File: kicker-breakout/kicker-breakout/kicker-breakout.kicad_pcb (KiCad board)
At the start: 2 copper layers, 43 x 37.8 mm, 16 parts, among them J1 POWER, J2 DEV_BOARD, J3 KICKER_CONNECTION, Q1 BSS84

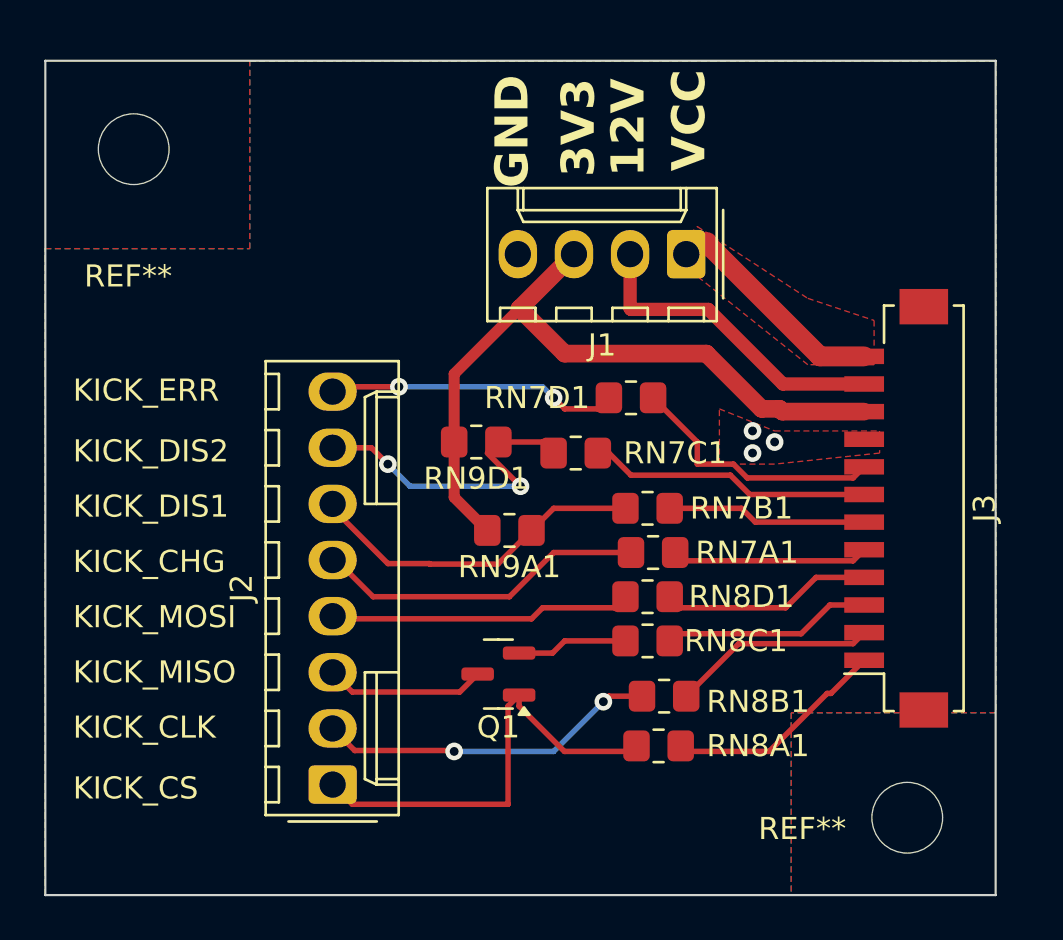
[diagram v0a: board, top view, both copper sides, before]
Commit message: Add jlpcb design rules and fix incorrect pullup value
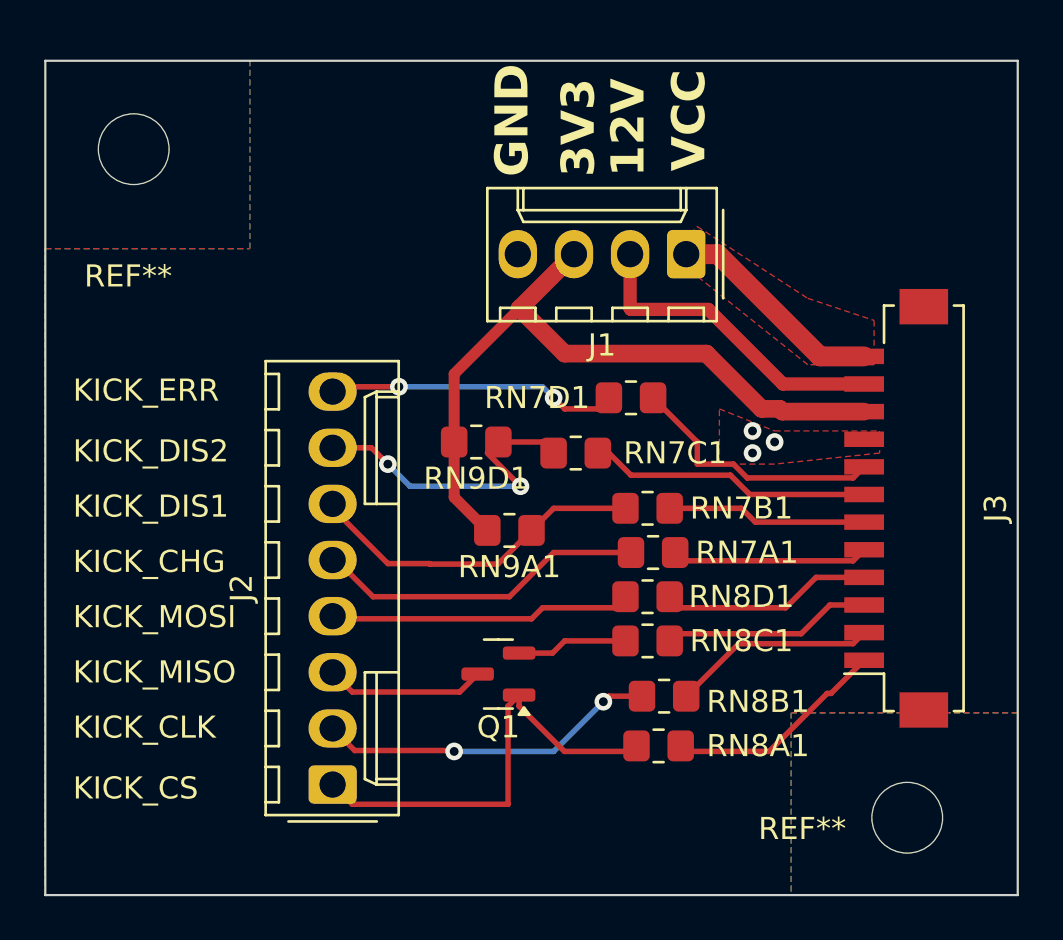
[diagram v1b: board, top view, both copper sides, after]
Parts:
- J1: value POWER -> 1x04_P2.54mm
- J2: value DEV_BOARD -> 1x08_P2.54mm
- J3: value KICKER_CONNECTION -> DF13C_CL535-0412-6-51_1x12-1MP_P1.25mm_Vertical
- RN9A1, RN9D1: value 100 -> 10k
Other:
- board size 43 x 37.8 mm -> 44 x 37.8 mm
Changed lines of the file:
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@@
 		(tags "resistor handsolder")
 		(property "Reference" "RN7C1"
-			(at 4.5 0 360)
+			(at 4.5 0 0)
 			(layer "F.SilkS")
 			(effects
@@
 		)
 		(property "Value" "100"
-			(at 0 1.65 360)
+			(at 0 1.65 0)
 			(layer "F.Fab")
 			(effects
@@
 		)
 		(fp_text user "${REFERENCE}"
-			(at 0 0 360)
+			(at 0 0 0)
 			(layer "F.Fab")
 			(effects
@@
 		(tags "resistor handsolder")
 		(property "Reference" "RN7D1"
-			(at -4.25 0 360)
+			(at -4.25 0 0)
 			(layer "F.SilkS")
 			(effects
@@
 		)
 		(property "Value" "100"
-			(at 0 -1.5 360)
+			(at 0 -1.5 0)
 			(layer "F.Fab")
 			(effects
@@
 		)
 		(fp_text user "${REFERENCE}"
-			(at 0 0 360)
+			(at 0 0 0)
 			(layer "F.Fab")
 			(effects
@@
 		(tags "resistor handsolder")
 		(property "Reference" "RN9A1"
-			(at 0 -1.65 360)
+			(at 0 -1.65 0)
 			(layer "F.SilkS")
 			(effects
@@
 			)
 		)
-		(property "Value" "100"
-			(at 0 1.65 360)
+		(property "Value" "10k"
+			(at 0 1.65 0)
 			(layer "F.Fab")
 			(effects
@@
 		)
 		(fp_text user "${REFERENCE}"
-			(at 0 0 360)
+			(at 0 0 0)
 			(layer "F.Fab")
 			(effects
@@
 		(tags "resistor handsolder")
 		(property "Reference" "RN8C1"
-			(at 4 0 0)
+			(at 4.25 0 0)
 			(layer "F.SilkS")
 			(effects
@@
 		(tags "resistor handsolder")
 		(property "Reference" "RN7B1"
-			(at 4.25 0 360)
+			(at 4.25 0 0)
 			(layer "F.SilkS")
 			(effects
@@
 		)
 		(property "Value" "100"
-			(at 0 1.65 360)
+			(at 0 1.65 0)
 			(layer "F.Fab")
 			(effects
@@
 		)
 		(fp_text user "${REFERENCE}"
-			(at 0 0 360)
+			(at 0 0 0)
 			(layer "F.Fab")
 			(effects
@@
 			)
 		)
-		(property "Value" "DEV_BOARD"
+		(property "Value" "1x08_P2.54mm"
 			(at 8.89 4.08 90)
 			(layer "F.Fab")
@@
 		)
 		(property "Value" "MountingHole_3.2mm_M3"
-			(at 0 4.2 0)
+			(at 0 7 0)
 			(layer "F.Fab")
 			(effects
@@
 		)
 		(property "Value" "MountingHole_3.2mm_M3"
-			(at 0 4.2 0)
+			(at 0.5 -5.25 0)
 			(layer "F.Fab")
 			(effects
@@
 		(tags "connector Hirose DF13C vertical")
 		(property "Reference" "J3"
-			(at 0 4 90)
+			(at 0 4.5 90)
 			(layer "F.SilkS")
 			(effects
@@
 			)
 		)
-		(property "Value" "KICKER_CONNECTION"
-			(at 0 4.15 90)
+		(property "Value" "DF13C_CL535-0412-6-51_1x12-1MP_P1.25mm_Vertical"
+			(at 0 7 90)
 			(layer "F.Fab")
 			(effects
@@
 		(tags "SOT TO_SOT_SMD")
 		(property "Reference" "Q1"
-			(at 0 -2.4 360)
+			(at 0 -2.4 0)
 			(layer "F.SilkS")
 			(effects
@@
 		)
 		(property "Value" "BSS84"
-			(at 0 2.4 360)
+			(at 0 2.4 0)
 			(layer "F.Fab")
 			(effects
@@
 		)
 		(property "Footprint" "Package_TO_SOT_SMD:SOT-23"
-			(at 0 0 360)
+			(at 0 0 0)
 			(layer "F.Fab")
 			(hide yes)
@@
 		)
 		(property "Datasheet" "http://assets.nexperia.com/documents/data-sheet/BSS84.pdf"
-			(at 0 0 360)
+			(at 0 0 0)
 			(layer "F.Fab")
 			(hide yes)
@@
 		)
 		(property "Description" "-0.13A Id, -50V Vds, P-Channel MOSFET, SOT-23"
-			(at 0 0 360)
+			(at 0 0 0)
 			(layer "F.Fab")
 			(hide yes)
@@
 		)
 		(fp_text user "${REFERENCE}"
-			(at 0 0 360)
+			(at 0 0 0)
 			(layer "F.Fab")
 			(effects
@@
 		(tags "resistor handsolder")
 		(property "Reference" "RN7A1"
-			(at 4.25 0 360)
+			(at 4.25 0 0)
 			(layer "F.SilkS")
 			(effects
@@
 		)
 		(property "Value" "100"
-			(at 0 1.65 360)
+			(at 0 1.65 0)
 			(layer "F.Fab")
 			(effects
@@
 		)
 		(fp_text user "${REFERENCE}"
-			(at 0 0 360)
+			(at 0 0 0)
 			(layer "F.Fab")
 			(effects
@@
 		)
 		(property "Value" "100"
-			(at -27.5 11.2 0)
+			(at -3.25 0 0)
 			(layer "F.Fab")
 			(effects
@@
 		(tags "connector Molex KK-254 vertical")
 		(property "Reference" "J1"
-			(at 3.81 -4.12 360)
+			(at 3.81 -4.12 0)
 			(layer "F.SilkS")
 			(effects
@@
 			)
 		)
-		(property "Value" "POWER"
-			(at 3.81 4.08 360)
+		(property "Value" "1x04_P2.54mm"
+			(at 3.81 4.08 0)
 			(layer "F.Fab")
 			(effects
@@
 		)
 		(fp_text user "${REFERENCE}"
-			(at 3.81 -2.22 360)
+			(at 3.81 -2.22 0)
 			(layer "F.Fab")
 			(effects
@@
 		(tags "resistor handsolder")
 		(property "Reference" "RN9D1"
-			(at 0 -1.65 360)
+			(at 0 -1.65 0)
 			(layer "F.SilkS")
 			(effects
@@
 			)
 		)
-		(property "Value" "100"
-			(at 0 1.65 360)
+		(property "Value" "10k"
+			(at 0 1.65 0)
 			(layer "F.Fab")
 			(effects
@@
 		)
 		(fp_text user "${REFERENCE}"
-			(at 0 0 360)
+			(at 0 0 0)
 			(layer "F.Fab")
 			(effects
@@
 	(gr_rect
 		(start 136 53.25)
-		(end 179 91)
+		(end 180 91)
 		(stroke
 			(width 0.1)
@@
 	)
 	(gr_text "GND"
-		(at 158 59 90)
+		(at 158 58.5 90)
 		(layer "F.SilkS")
 		(effects
@@
 	)
 	(segment
-		(start 165.925 61.5)
+		(start 166.425 62)
 		(end 171.05 66.625)
 		(width 0.9)
@@
 	)
 	(segment
-		(start 171.05 66.625)
-		(end 173.05 66.625)
-		(width 0.9)
-		(layer "F.Cu")
-		(net 3)
-	)
-	(segment
 		(start 165 62)
-		(end 165.5 61.5)
-		(width 1)
+		(end 166.425 62)
+		(width 0.9)
 		(layer "F.Cu")
 		(net 3)
 	)
 	(segment
-		(start 165.5 61.5)
-		(end 165.925 61.5)
-		(width 1)
+		(start 171.05 66.625)
+		(end 173.05 66.625)
+		(width 0.9)
 		(layer "F.Cu")
 		(net 3)
@@
 			(thermal_gap 0.5)
 			(thermal_bridge_width 0.5)
-			(island_removal_mode 1)
-			(island_area_min 10)
 		)
 		(polygon
 			(pts
-				(xy 136 61.75) (xy 145.25 61.75) (xy 145.25 53.25) (xy 179 53.25) (xy 179 82.75) (xy 169.75 82.75)
+				(xy 136 61.75) (xy 145.25 61.75) (xy 145.25 53.25) (xy 180 53.25) (xy 180 82.75) (xy 169.75 82.75)
 				(xy 169.75 91) (xy 136 91)
 			)
@@
 		(layer "F.Cu")
 		(hatch edge 0.5)
-		(priority 2)
+		(priority 4)
 		(connect_pads
 			(clearance 0.5)
@@
 		(polygon
 			(pts
-				(xy 136 61.75) (xy 145.25 61.75) (xy 145.25 53.25) (xy 179 53.25) (xy 179 82.75) (xy 169.75 82.75)
+				(xy 136 61.75) (xy 145.25 61.75) (xy 145.25 53.25) (xy 180 53.25) (xy 180 82.75) (xy 169.75 82.75)
 				(xy 169.75 91) (xy 136 91)
 			)
